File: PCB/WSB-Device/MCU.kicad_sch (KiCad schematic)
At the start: 44 parts, among them J1 Conn_02x04_Counter_Clockwise, J2 Conn_01x08, SW1 SW_SPST_4_PIN, U1 ESP32-C6FH4, U5 74LV1T34, Y3 Crystal_GND24

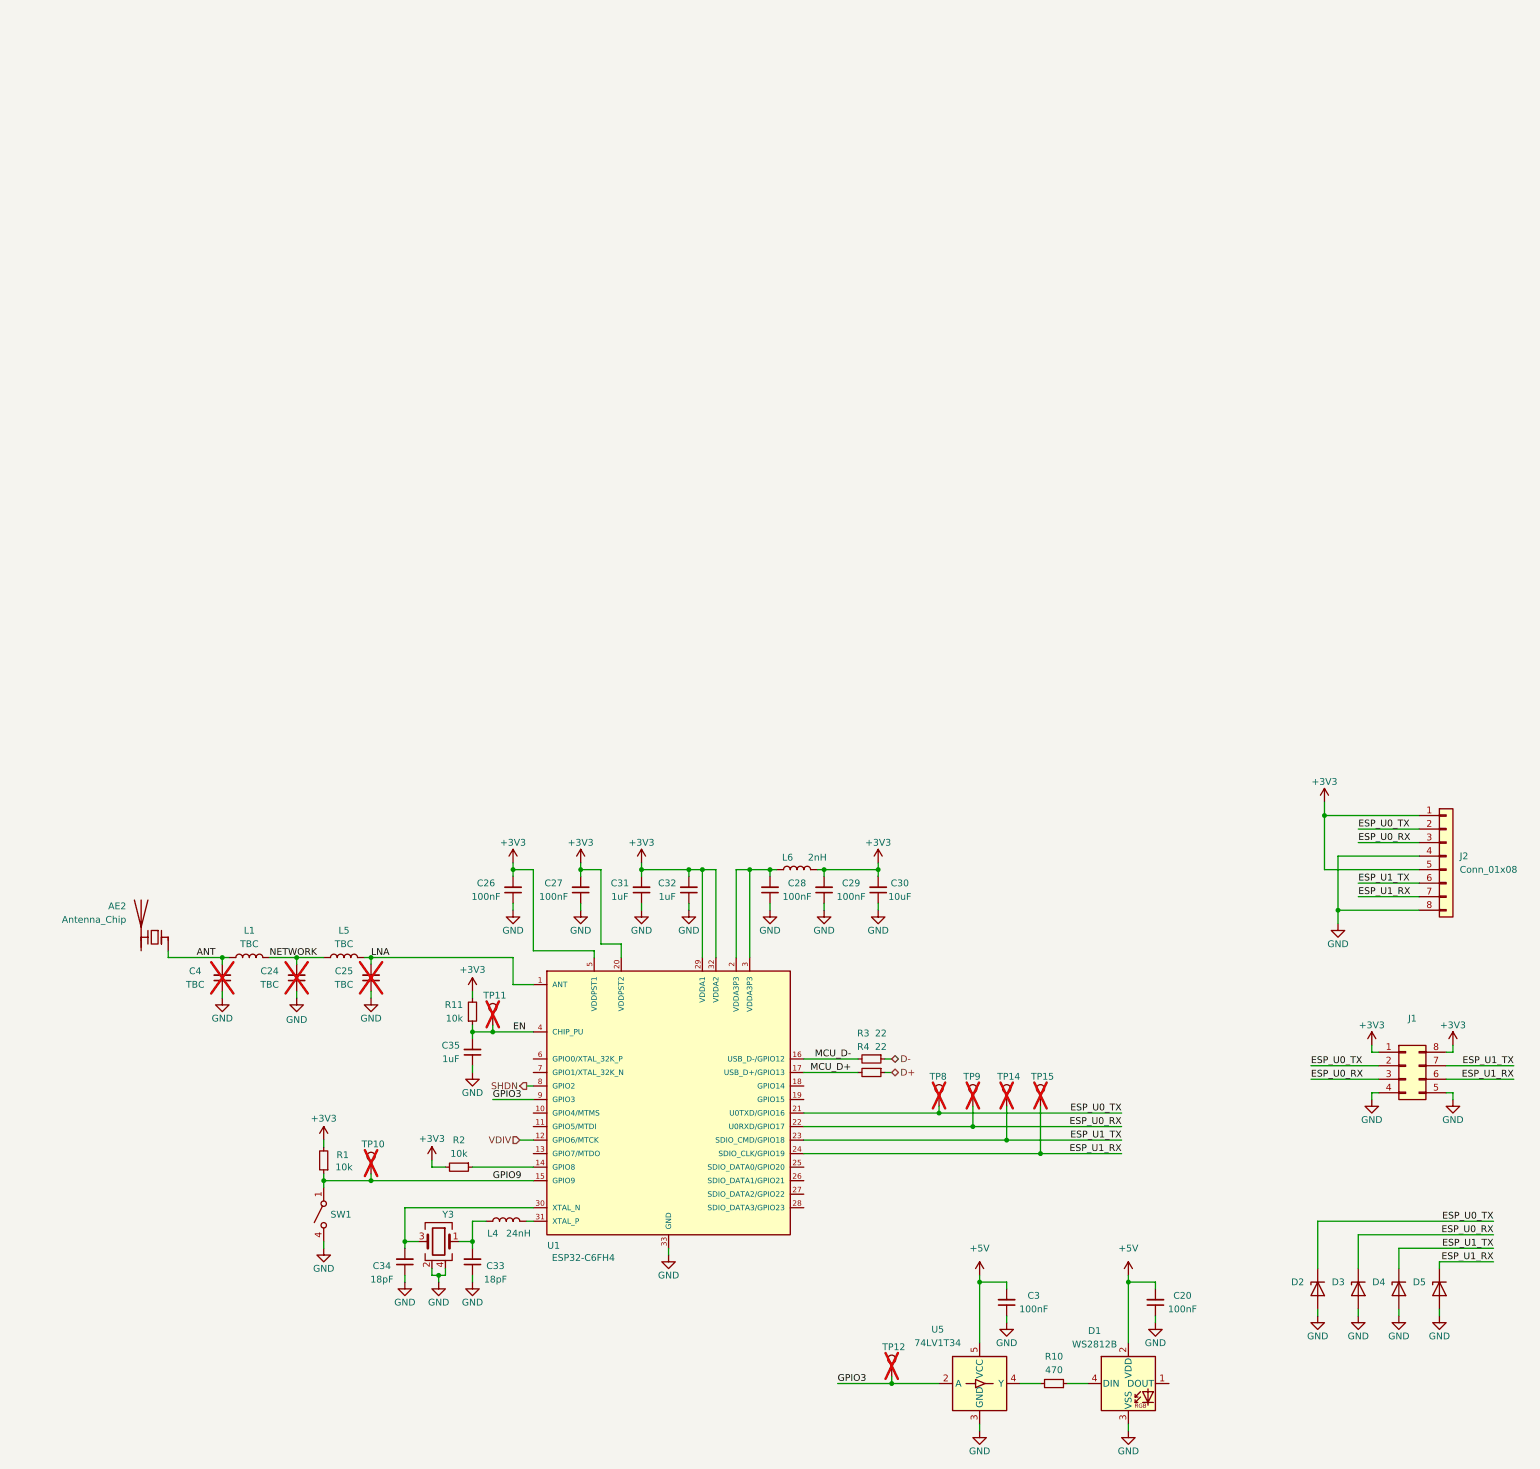
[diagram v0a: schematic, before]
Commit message: -Corrected test point numbering
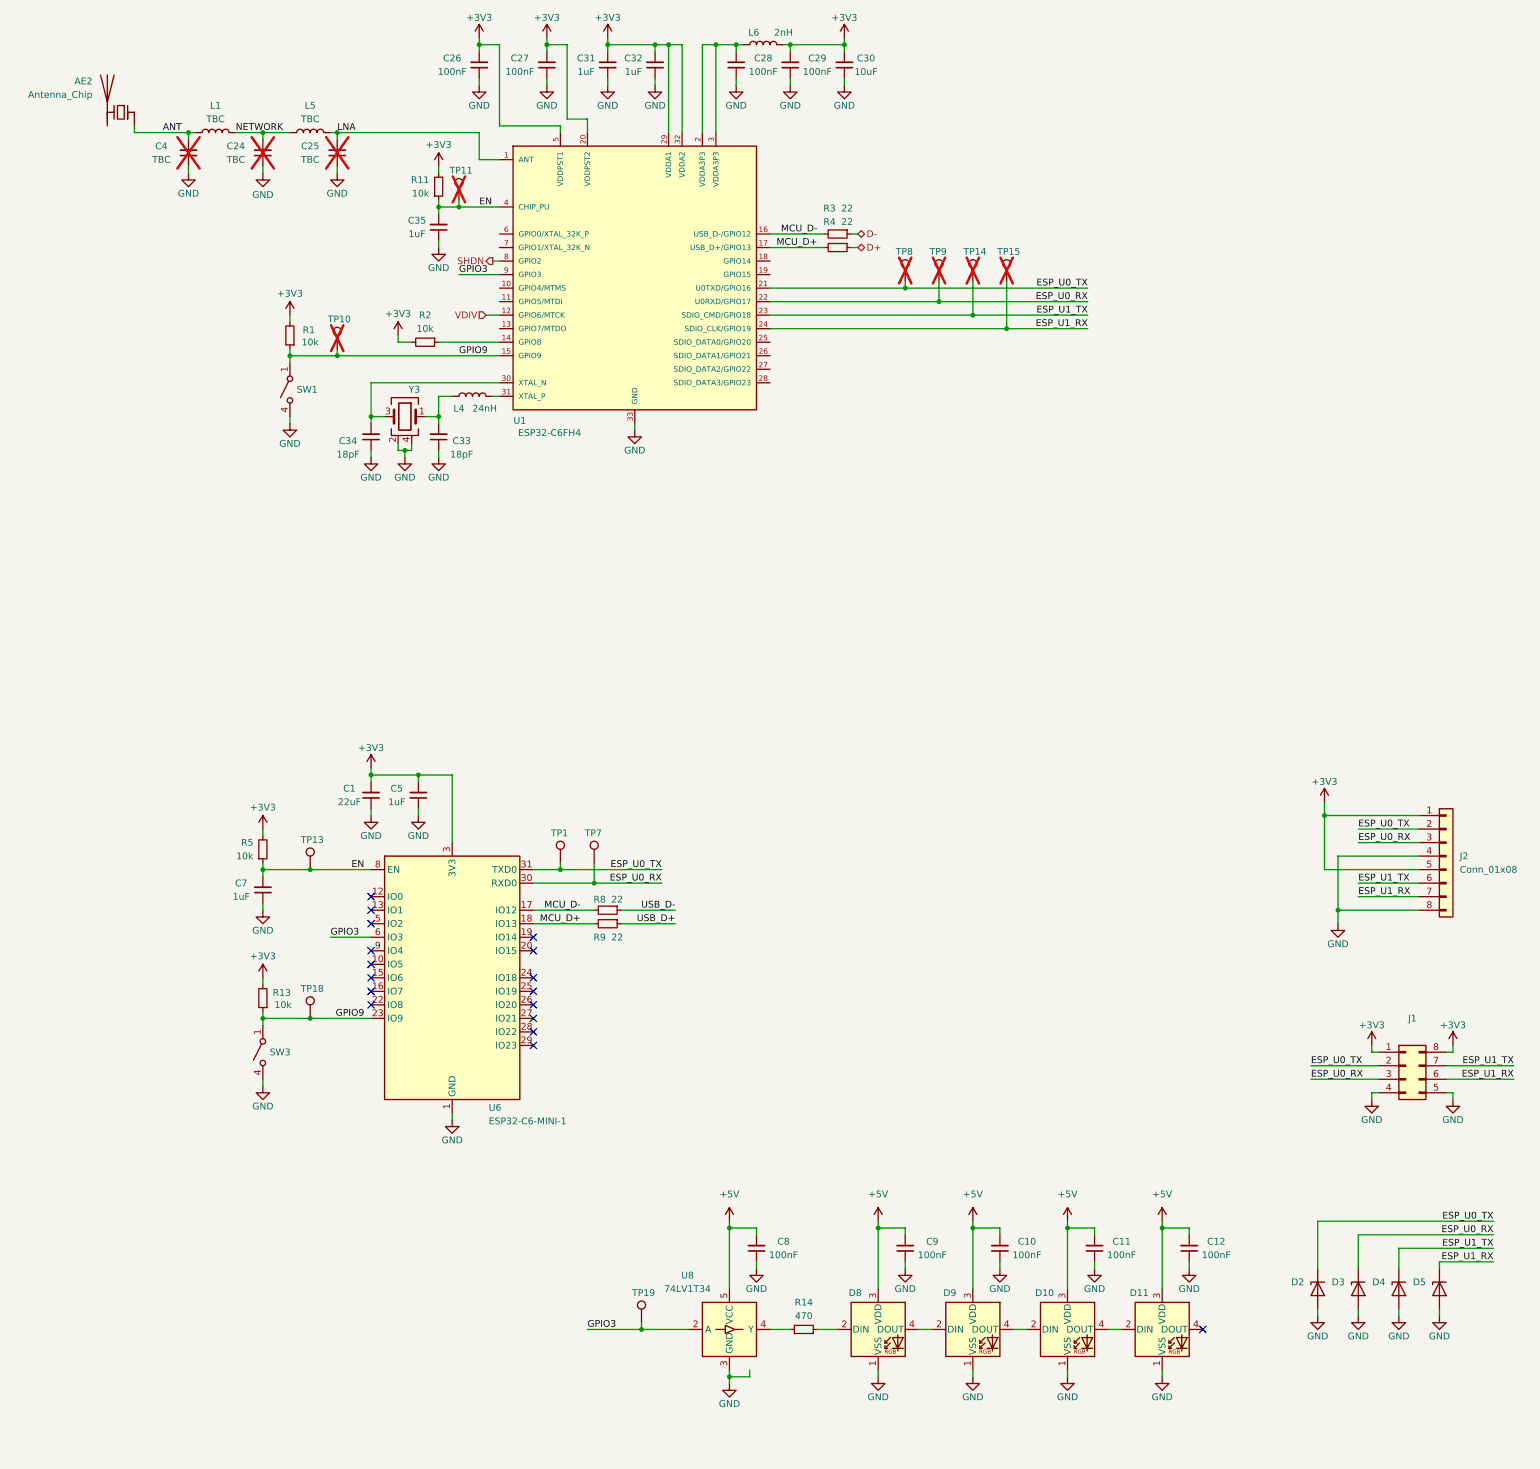
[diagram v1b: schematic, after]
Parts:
- removed C20, C3: 100nF, Capacitor_SMD:C_0402_1005Metric, symbol Device:C_Small
- removed D1: WS2812B, EN_Designs-Footprints:XL-1010RGBC-WS2812B, symbol EN_Designs-Symbols:WS2812B Alternate Pinout
- removed R10: 470, Resistor_SMD:R_0402_1005Metric, symbol Device:R_Small
- removed TP12: TestPoint, TestPoint:TestPoint_Pad_D1.0mm, symbol Connector:TestPoint
- removed U5: 74LV1T34, EN_Designs-Footprints:X2SON5_0.8x0.8mm_SOT1226, symbol EN_Designs-Symbols:74LV1T34
- added C1: 22uF, Capacitor_SMD:C_0603_1608Metric, symbol Device:C_Small
- added C10, C11, C12, C8, C9: 100nF, Capacitor_SMD:C_0201_0603Metric, symbol Device:C_Small
- added C5, C7: 1uF, Capacitor_SMD:C_0402_1005Metric, symbol Device:C_Small
- added D10, D11, D8, D9: (no value), EN_Designs-Footprints:XL-3210RGBC-2812B, symbol LED:SK6812
- added R13, R5: 10k, Resistor_SMD:R_0201_0603Metric, symbol Device:R_Small
- added R14: 470, Resistor_SMD:R_0201_0603Metric, symbol Device:R_Small
- added R8, R9: 22, Resistor_SMD:R_0201_0603Metric, symbol Device:R_Small
- added SW3: SW_SPST_4_PIN, EN_Designs-Footprints:1TS026A-2300-0553-CT, symbol EN_Designs-Symbols:SW_SPST_4_PIN
- added TP1, TP13, TP18, TP19, TP7: TestPoint, EN_Designs-Footprints:TestPoint_Pad_D1.0mm, symbol Connector:TestPoint
- added U6: ESP32-C6-MINI-1, RF_Module:ESP32-C6-MINI-1, symbol RF_Module:ESP32-C6-MINI-1
- added U8: 74LV1T34, EN_Designs-KiCad-Lib:X2SON5_0.8x0.8mm_SOT1226, symbol EN_Designs-Symbols:74LV1T34
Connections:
- net +3V3: now also C1.2, C5.2, R13.2, R5.2, U6.3 (3V3)
- net +5V: now also C10.2, C11.2, C12.2, C8.2, C9.2, D10.3 (VDD), D11.3 (VDD), D8.3 (VDD), D9.3 (VDD), U8.5 (VCC)
- net EN: now also C7.2, R5.1, TP13.1, U6.8 (EN)
- net ESP_U0_RX: now also TP7.1, U6.30 (RXD0)
- net ESP_U0_TX: now also TP1.1, U6.31 (TXD0)
- net GND: now also C1.1, C10.1, C11.1, C12.1, C5.1, C7.1, C8.1, C9.1, D10.1 (VSS), D11.1 (VSS), D8.1 (VSS), D9.1 (VSS), SW3.3 (B), SW3.4 (B), U6.1 (GND), U6.11 (GND), U6.14 (GND), U6.2 (GND), U6.36 (GND), U6.37 (GND), U6.38 (GND), U6.39 (GND), U6.40 (GND), U6.41 (GND), U6.42 (GND), U6.43 (GND), U6.44 (GND), U6.45 (GND), U6.46 (GND), U6.47 (GND), U6.48 (GND), U6.49 (GND), U6.50 (GND), U6.51 (GND), U6.52 (GND), U6.53 (GND), U8.3 (GND)
- net GPIO3: now also TP19.1, U6.6 (IO3), U8.2 (A)
- net GPIO9: now also R13.1, SW3.1 (A), SW3.2 (A), TP18.1, U6.23 (IO9)
- net MCU_D+: now also R9.2, U6.18 (IO13)
- net MCU_D-: now also R8.2, U6.17 (IO12)
- new net: D8.2 (DIN), R14.1
- new net: D8.4 (DOUT), D9.2 (DIN)
- new net: D10.4 (DOUT), D11.2 (DIN)
- new net: D10.2 (DIN), D9.4 (DOUT)
- new net: R14.2, U8.4 (Y)
- new net USB_D+: R9.1
- new net USB_D-: R8.1
- no-connect marks 0 -> 17
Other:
- moved on the sheet: AE2, C24, C25, C26, C27, C28, C29, C30, C31, C32, C33, C34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
